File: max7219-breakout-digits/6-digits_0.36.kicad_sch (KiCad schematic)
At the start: 5 parts, among them J1 Conn_02x08_Odd_Even, U1 HDSM-443B_7-Segment_2_Digit, U2 HDSM-443B_7-Segment_2_Digit

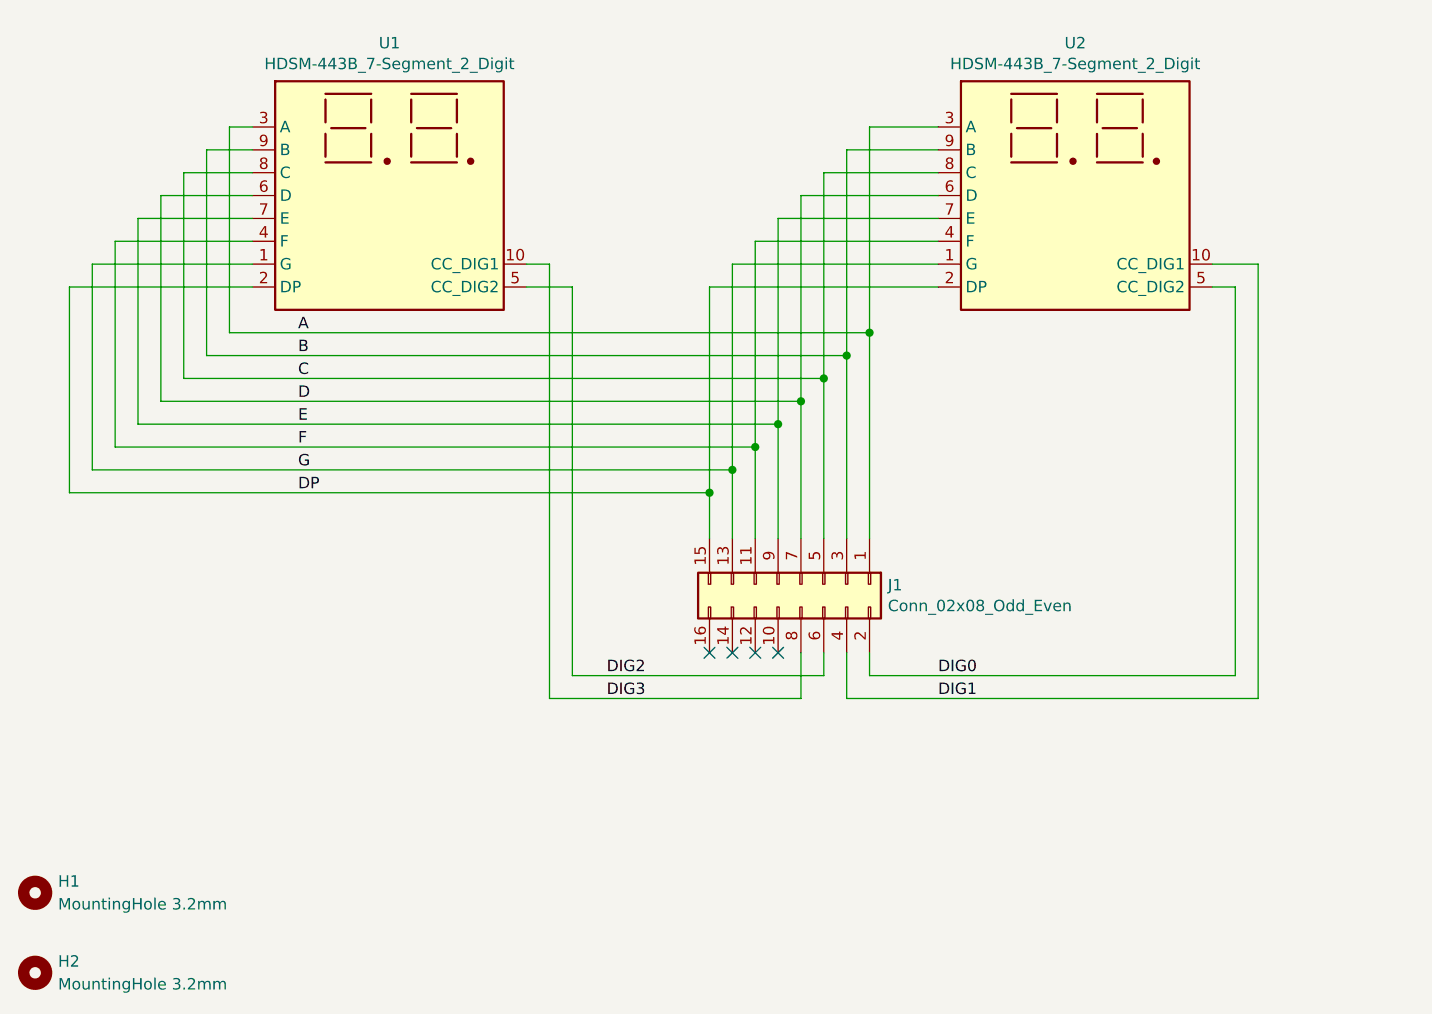
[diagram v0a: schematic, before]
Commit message: rename everything from 0.35 to 0.36
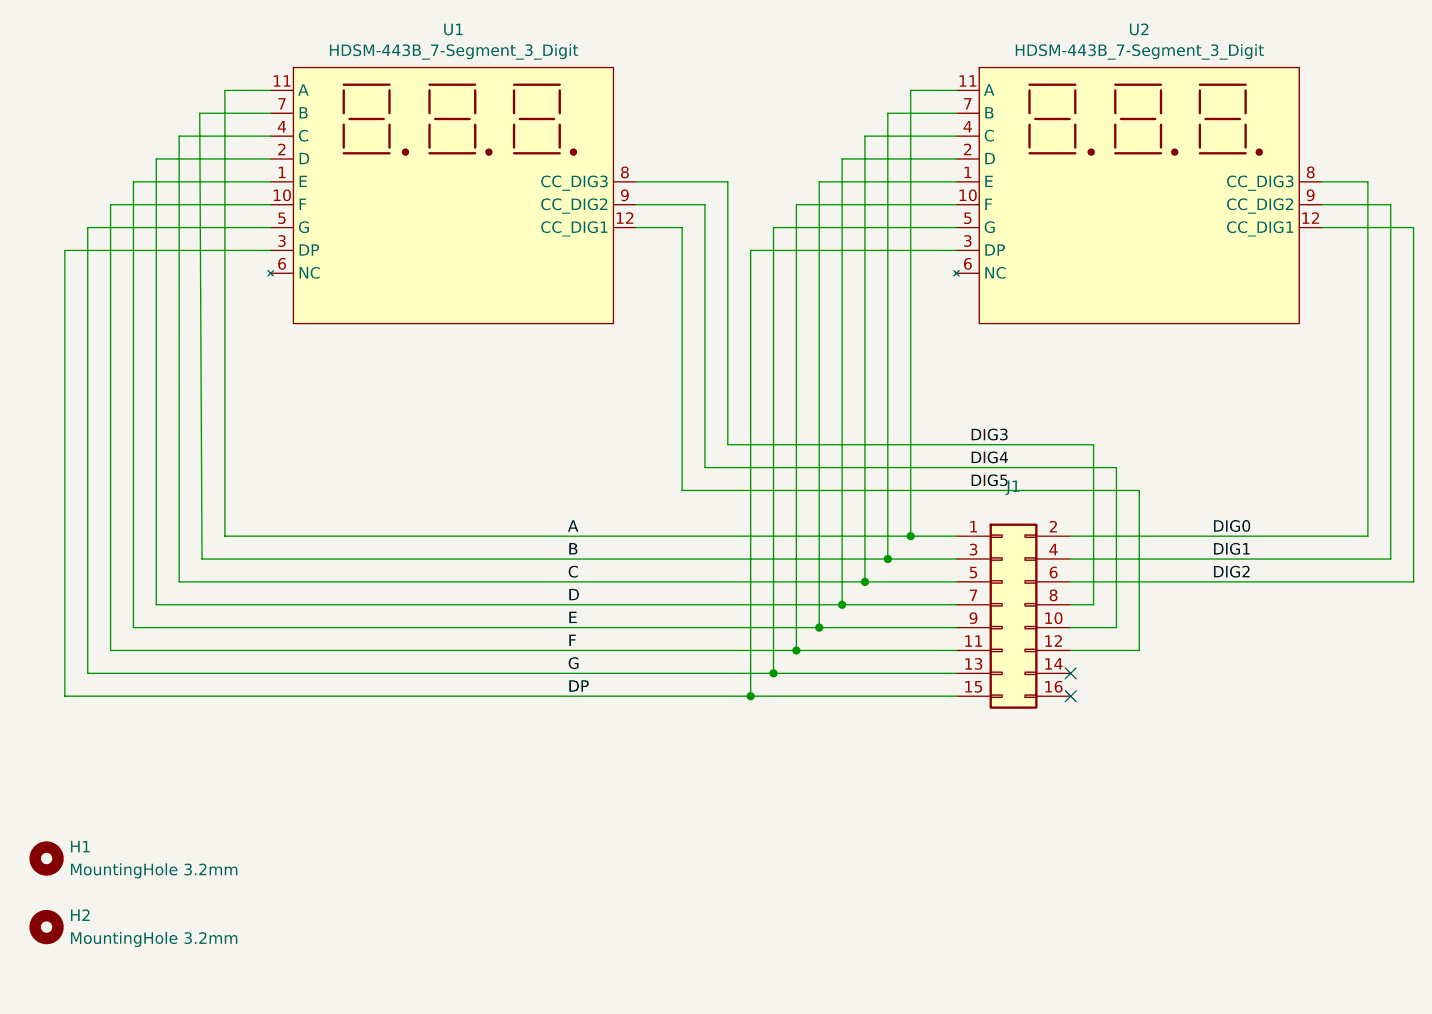
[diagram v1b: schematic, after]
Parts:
- removed U1, U2: HDSM-443B_7-Segment_2_Digit, MobiFlight:STH_7_2 Digits_0.35_CC, symbol MobiFlight:7Segment 2 digit 0.35 common cathode STH
- added U1, U2: HDSM-443B_7-Segment_3_Digit, MobiFlight:STH_7_3 Digits_0.36_CC, symbol MobiFlight:7Segment 3 digit 0.36 common cathode STH
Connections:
- net A: now also U1.11 (A), U2.11 (A)
- net B: now also U1.7 (B), U2.7 (B)
- net C: now also U1.4 (C), U2.4 (C)
- net D: now also U1.2 (D), U2.2 (D)
- net DIG0: now also U2.8 (CC_DIG3)
- net DIG1: now also U2.9 (CC_DIG2)
- net DIG2: now also U2.12 (CC_DIG1)
- net DIG3: now also U1.8 (CC_DIG3)
- net DP: now also U1.3 (DP), U2.3 (DP)
- net E: now also U1.1 (E), U2.1 (E)
- net F: now also U1.10 (F), U2.10 (F)
- net G: now also U1.5 (G), U2.5 (G)
- net DIG4: now reaches J1.10 (Pin_10)
- net DIG4: now also U1.9 (CC_DIG2)
- net DIG5: now reaches J1.12 (Pin_12)
- net DIG5: now also U1.12 (CC_DIG1)
- no-connect marks 4 -> 2
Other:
- title: 7-Segment Display Module 0.35, 4 Digits -> 7-Segment Display Module 0.36, 6 Digits
